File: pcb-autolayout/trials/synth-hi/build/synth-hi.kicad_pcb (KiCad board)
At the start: 4 copper layers, 52 x 40 mm, 74 parts, among them J1 CONN, U1 MCU, U11 BUF, U12 BUF, U13 BUF, U14 BUF, U15 BUF, U16 BUF, U17 BUF, U18 BUF, U19 BUF, U2 LDO, U20 BUF, U21 BUF, U22 BUF, Y1 8MHz

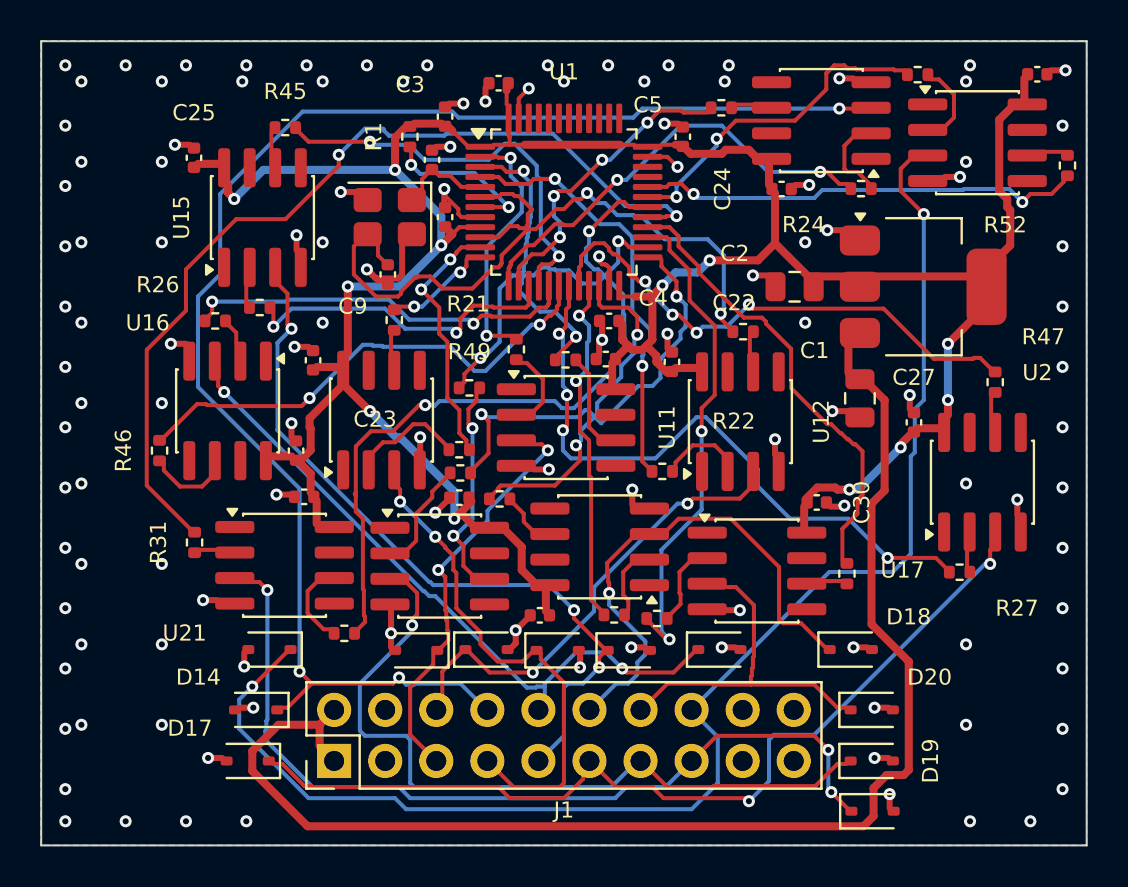
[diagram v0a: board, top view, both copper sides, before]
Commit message: synth-hi: build sau chốt chống chập — DRC 0 (hết 15 chập), 5 chân hở MCU minh bạch
Co-Authored-By: Claude Opus 5.5 <noreply@anthropic.com>
Claude-Session: https://claude.ai/code/session_012jwodCpQFB8wopi3P3TnUz
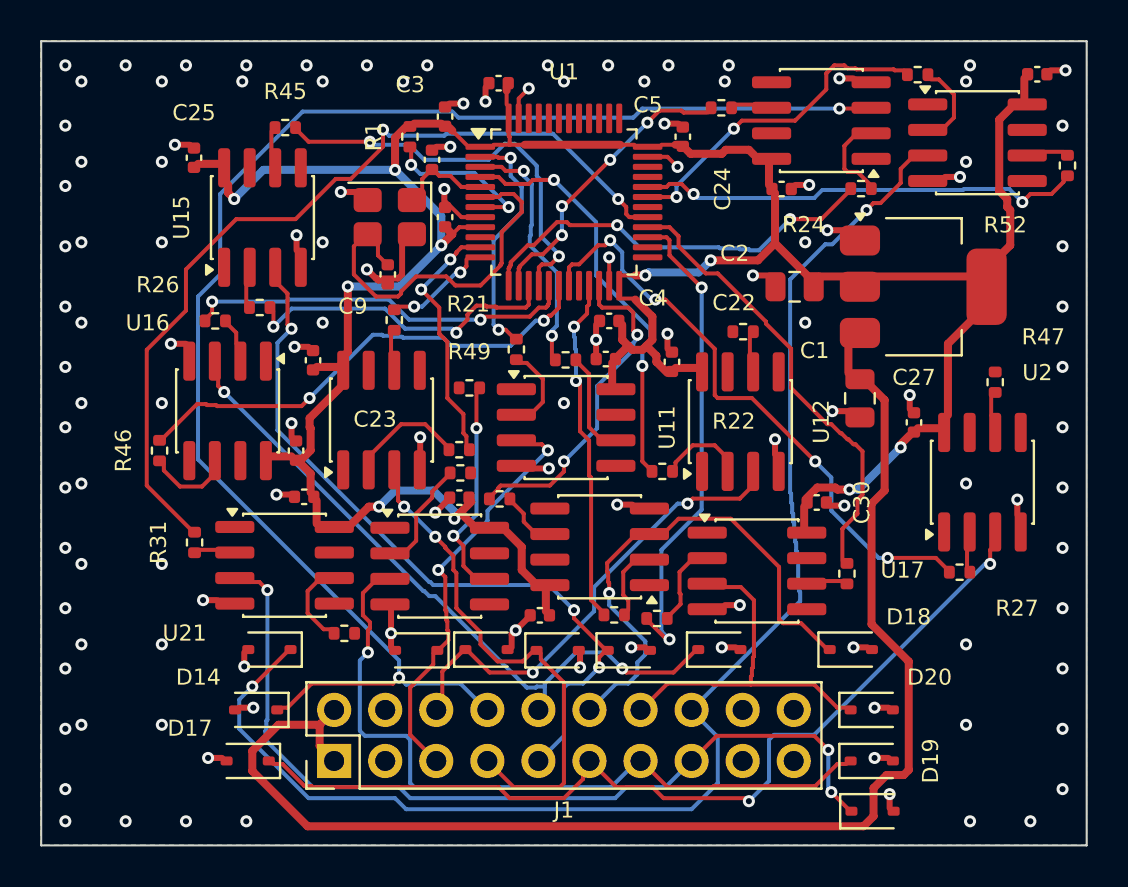
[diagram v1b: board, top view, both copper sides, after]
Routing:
- net S11_B: track 35.2 -> 0.00 mm, vias 2 -> 0
- net S7_B: track 25.7 -> 0.00 mm, vias 4 -> 0
- net S9_A: track 20.4 -> 0.00 mm, vias 2 -> 0
- net S2_B: track 17.6 -> 0.00 mm, vias 2 -> 0
- net S9_B: track 14.7 -> 0.00 mm, vias 2 -> 0
- net S11_A: track 44.9 -> 42.4 mm
- net S7_A: track 31.6 -> 29.2 mm
- net S12_OUT: track 68.8 -> 66.8 mm
- net +3V3: track 121.8 -> 120.0 mm, vias 12 -> 10
- net S4_OUT: track 71.8 -> 73.3 mm, vias 3 -> 2
- net S4_A: track 21.4 -> 19.9 mm
- net S1_B: track 13.1 -> 11.7 mm
- net S9_OUT: track 36.0 -> 35.2 mm
- net S1_A: track 11.9 -> 11.1 mm
- net S4_B: track 14.5 -> 13.8 mm
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
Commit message: T34 trên synth-hi: 5 -> 2 chân hở (vành thoát chân U1 0.8 mm), DRC 0; router in thời gian theo pha
Vành 1.6 mm tệ hơn (3 chân hở) -> engine giữ kết quả tốt nhất. Tổng 47 phút: quá chậm, đang profile.

Co-Authored-By: Claude Opus 5.5 <noreply@anthropic.com>
Claude-Session: https://claude.ai/code/session_012jwodCpQFB8wopi3P3TnUz
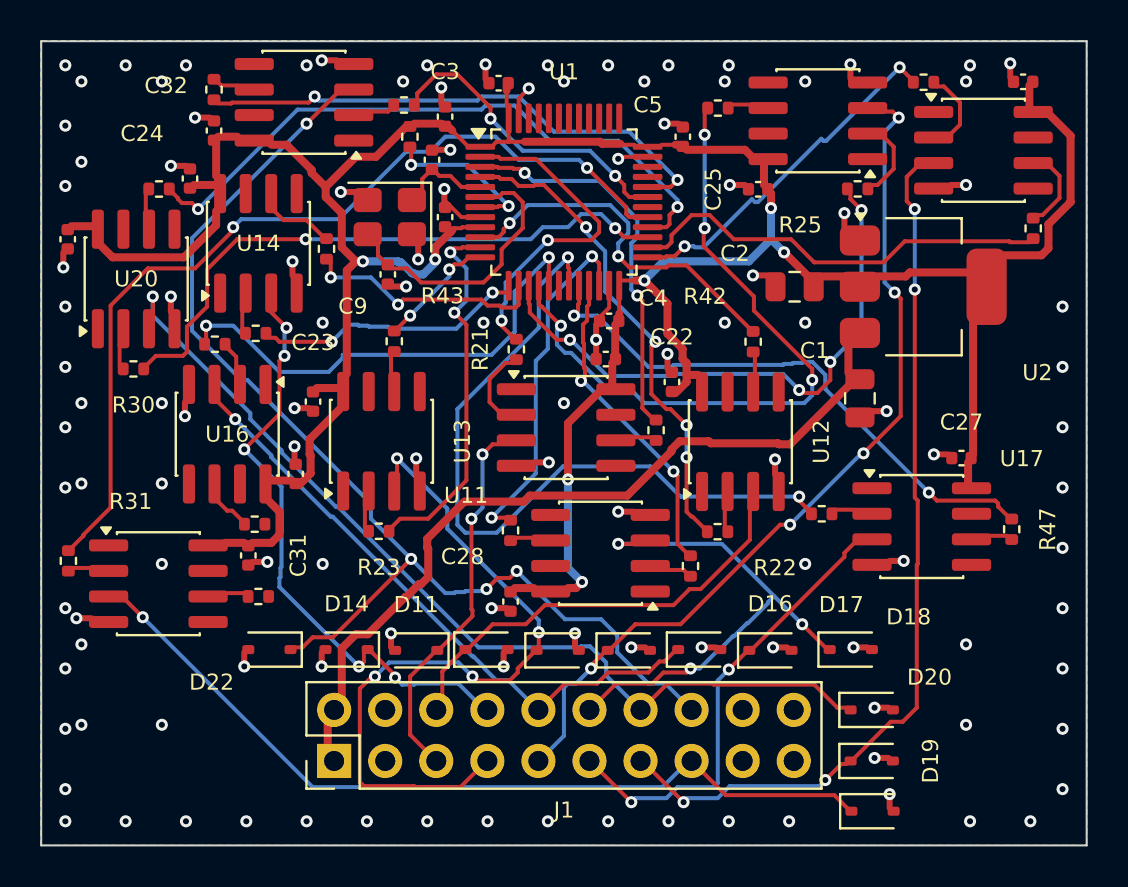
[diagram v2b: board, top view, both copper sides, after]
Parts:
- C23: renamed from C8; value 12p -> 100n
- C26: renamed from C9; value 12p -> 100n
- C7: renamed from C6; value 100n -> 1u
- C8: renamed from C7; value 1u -> 12p
- C9: renamed from C3; value 100n -> 12p
- R1: renamed from R21; value 33R -> 10k
- R22: renamed from R44; value 1k -> 33R
- R24: renamed from R43; value 1k -> 33R
- R26: renamed from R45; value 1k -> 33R
- R31: renamed from R46; value 1k -> 33R
- R32: renamed from R48; value 1k -> 33R
- R41: renamed from R30; value 33R -> 1k
- R44: renamed from R23; value 33R -> 1k
- R50: renamed from R26; value 33R -> 1k
- R51: renamed from R1; value 10k -> 1k
- R52: renamed from R25; value 33R -> 1k
- moved C6 26.5 mm to (122.8, 62.1)
- moved R29 24.4 mm to (143.9, 62.0)
- moved R51 24.1 mm to (110.8, 87.6), turned to 0 degrees
- moved U22 24.0 mm to (113.1, 63.0), turned to 180 degrees
- moved R22 21.1 mm to (133.6, 84.4), turned to 0 degrees
- moved R32 20.2 mm to (118.0, 63.2)
- moved U17 19.3 mm to (143.8, 84.1)
- moved C3 19.0 mm to (120.1, 63.8), turned to 90 degrees
- moved U21 18.9 mm to (105.8, 87.0), turned to 0 degrees
- moved C32 18.8 mm to (108.6, 64.4), turned to 90 degrees
- moved U19 16.5 mm to (146.9, 65.4), turned to 0 degrees
- moved R27 16.3 mm to (138.8, 83.5)
- moved C25 15.8 mm to (135.7, 67.4), turned to 180 degrees
- moved C24 14.5 mm to (107.4, 66.8)
- moved R21 14.1 mm to (123.6, 75.3), turned to -90 degrees
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- renumbered C4 to C21, C5 to C22, C26 to C24, C30 to C25, C21 to C28, C32 to C29, C29 to C3, C25 to C30, C23 to C31, C31 to C32, C22 to C4, C24 to C5, C28 to C6, D22 to D11, D11 to D12, D12 to D13, D13 to D15, D15 to D16, D16 to D17, D17 to D22, R28 to R21, R29 to R23, R32 to R25, R24 to R27, R22 to R28, R27 to R29, R31 to R30, R50 to R42, R49 to R43, R42 to R45, R51 to R46, R41 to R48, R52 to R49, U18 to U11, U20 to U12, U11 to U13, U13 to U14, U14 to U15, U21 to U16, U22 to U17, U12 to U18, U17 to U19, U16 to U20, U15 to U21, U19 to U22
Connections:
- C23 pad 1: OSC_IN -> +3V3
- C26 pad 1: OSC_OUT -> +3V3
- C8 pad 1: +3V3 -> OSC_IN
- C9 pad 1: +3V3 -> OSC_OUT
- D11 pad 1: S12_OUT -> S1_OUT
- D12 pad 1: S1_OUT -> S2_OUT
- D13 pad 1: S2_OUT -> S3_OUT
- D15 pad 1: S3_OUT -> S5_OUT
- D16 pad 1: S5_OUT -> S6_OUT
- D17 pad 1: S6_OUT -> S7_OUT
- D22 pad 1: S7_OUT -> S12_OUT
- R1 pad 1: S1_A -> NRST
- R1 pad 2: S1_IN -> +3V3
- R21 pad 1: S8_A -> S1_A
- R21 pad 2: S8_IN -> S1_IN
- R22 pad 1: S4_FB -> S2_A
- R22 pad 2: S4_B -> S2_IN
- R23 pad 1: S9_A -> S3_A
- R23 pad 2: S9_IN -> S3_IN
- R24 pad 1: S3_FB -> S4_A
- R24 pad 2: S3_B -> S4_IN
- R25 pad 1: S12_A -> S5_A
- R25 pad 2: S12_IN -> S5_IN
- R26 pad 1: S5_FB -> S6_A
- R26 pad 2: S5_B -> S6_IN
- R27 pad 1: S4_A -> S7_A
- R27 pad 2: S4_IN -> S7_IN
- R28 pad 1: S2_A -> S8_A
- R28 pad 2: S2_IN -> S8_IN
- R29 pad 1: S7_A -> S9_A
- R29 pad 2: S7_IN -> S9_IN
- R30 pad 1: S11_A -> S10_A
- R30 pad 2: S11_IN -> S10_IN
- R31 pad 1: S6_FB -> S11_A
- R31 pad 2: S6_B -> S11_IN
- R32 pad 1: S8_FB -> S12_A
- R32 pad 2: S8_B -> S12_IN
- R41 pad 1: S10_A -> S1_FB
- R41 pad 2: S10_IN -> S1_B
- R42 pad 1: S10_FB -> S2_FB
- R42 pad 2: S10_B -> S2_B
- R43 pad 1: S9_FB -> S3_FB
- R43 pad 2: S9_B -> S3_B
- R44 pad 1: S3_A -> S4_FB
- R44 pad 2: S3_IN -> S4_B
- R45 pad 1: S2_FB -> S5_FB
- R45 pad 2: S2_B -> S5_B
- R46 pad 1: S11_FB -> S6_FB
- R46 pad 2: S11_B -> S6_B
- R48 pad 1: S1_FB -> S8_FB
- R48 pad 2: S1_B -> S8_B
- R49 pad 1: S12_FB -> S9_FB
- R49 pad 2: S12_B -> S9_B
- R50 pad 1: S6_A -> S10_FB
- R50 pad 2: S6_IN -> S10_B
- R51 pad 1: NRST -> S11_FB
- R51 pad 2: +3V3 -> S11_B
- R52 pad 1: S5_A -> S12_FB
- R52 pad 2: S5_IN -> S12_B
- U11 pad 2: S8_IN -> S1_IN
- U11 pad 3: S8_OUT -> S1_OUT
- U11 pad 6: S8_FB -> S1_FB
- U12 pad 2: S10_IN -> S2_IN
- U12 pad 3: S10_OUT -> S2_OUT
- U12 pad 6: S10_FB -> S2_FB
- U13 pad 2: S1_IN -> S3_IN
- U13 pad 3: S1_OUT -> S3_OUT
- U13 pad 6: S1_FB -> S3_FB
- U14 pad 2: S3_IN -> S4_IN
- U14 pad 3: S3_OUT -> S4_OUT
- U14 pad 6: S3_FB -> S4_FB
- U15 pad 2: S4_IN -> S5_IN
- U15 pad 3: S4_OUT -> S5_OUT
- U15 pad 6: S4_FB -> S5_FB
- U16 pad 2: S11_IN -> S6_IN
- U16 pad 3: S11_OUT -> S6_OUT
- U16 pad 6: S11_FB -> S6_FB
- U17 pad 2: S12_IN -> S7_IN
- U17 pad 3: S12_OUT -> S7_OUT
- U17 pad 6: S12_FB -> S7_FB
- U18 pad 2: S2_IN -> S8_IN
- U18 pad 3: S2_OUT -> S8_OUT
- U18 pad 6: S2_FB -> S8_FB
- U19 pad 2: S7_IN -> S9_IN
- U19 pad 3: S7_OUT -> S9_OUT
- U19 pad 6: S7_FB -> S9_FB
- U20 pad 2: S6_IN -> S10_IN
- U20 pad 3: S6_OUT -> S10_OUT
- U20 pad 6: S6_FB -> S10_FB
- U21 pad 2: S5_IN -> S11_IN
- U21 pad 3: S5_OUT -> S11_OUT
- U21 pad 6: S5_FB -> S11_FB
- U22 pad 2: S9_IN -> S12_IN
- U22 pad 3: S9_OUT -> S12_OUT
- U22 pad 6: S9_FB -> S12_FB
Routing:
- net S4_OUT: track 73.3 -> 28.8 mm, vias 2 -> 5
- net S10_OUT: track 16.8 -> 45.1 mm, vias 0 -> 1
- net S7_B: track 0.00 -> 27.3 mm, vias 0 -> 2
- net VIN: track 64.3 -> 37.7 mm
- net S6_B: track 23.3 -> 0.00 mm, vias 2 -> 0
- net S7_OUT: track 44.3 -> 21.4 mm
- net S9_B: track 0.00 -> 20.6 mm
- net S2_B: track 0.00 -> 17.7 mm, vias 0 -> 2
- net S9_A: track 0.00 -> 16.8 mm, vias 0 -> 2
- net S5_B: track 19.7 -> 33.2 mm, vias 2 -> 4
- net S5_A: track 15.4 -> 27.8 mm, vias 2 -> 4
- net S3_OUT: track 23.6 -> 34.4 mm, vias 2 -> 4
- net S12_OUT: track 66.8 -> 56.5 mm, vias 2 -> 4
- net S10_B: track 21.9 -> 31.4 mm, vias 0 -> 2
- net S9_OUT: track 35.2 -> 42.9 mm, vias 1 -> 4
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
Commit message: bench R sau sửa review: bcm4l 16/16; synth-hi hết chập (DRC 21 -> 0) đổi 2 chân hở; synth-lo TỤT 0 -> 1 hở (đang truy)
bench ghi build/run.log từng trial để truy hồi quy.

Co-Authored-By: Claude Opus 5.5 <noreply@anthropic.com>
Claude-Session: https://claude.ai/code/session_012jwodCpQFB8wopi3P3TnUz
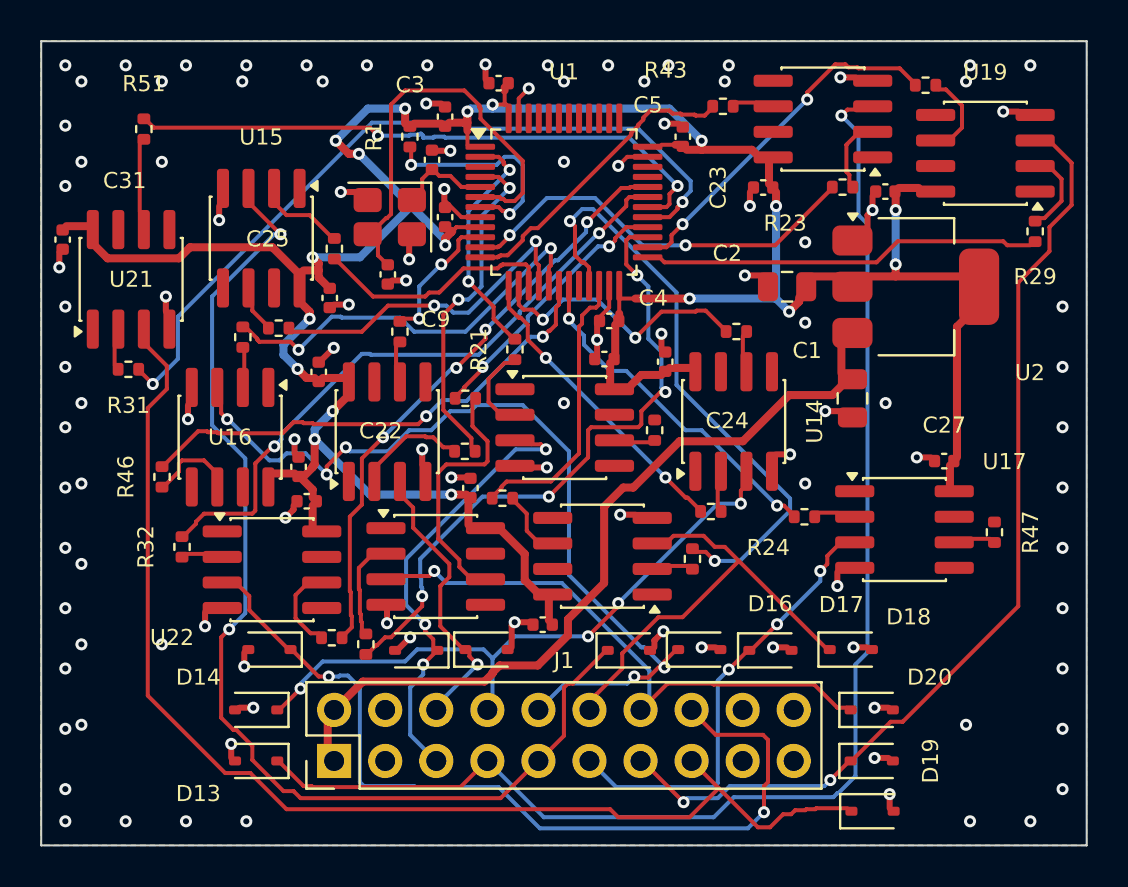
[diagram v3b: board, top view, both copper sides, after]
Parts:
- C3: renamed from C8; value 12p -> 100n
- C30: renamed from C7; value 1u -> 100n
- C7: renamed from C3; value 100n -> 1u
- C9: renamed from C23; value 100n -> 12p
- R1: renamed from R43; value 1k -> 10k
- R25: renamed from R51; value 1k -> 33R
- R29: renamed from R49; value 1k -> 33R
- R30: renamed from R44; value 1k -> 33R
- R32: renamed from R52; value 1k -> 33R
- R42: renamed from R23; value 33R -> 1k
- R49: renamed from R29; value 33R -> 1k
- R50: renamed from R1; value 10k -> 1k
- R51: renamed from R30; value 33R -> 1k
- R52: renamed from R24; value 33R -> 1k
- moved R32 22.8 mm to (107.0, 85.2)
- moved R30 19.8 mm to (116.1, 90.0), turned to 90 degrees
- moved C27 19.3 mm to (144.9, 80.9)
- moved C32 19.0 mm to (113.2, 82.9), turned to 180 degrees
- moved R25 17.7 mm to (114.6, 70.3), turned to 90 degrees
- moved R22 17.5 mm to (121.1, 80.4)
- moved U12 16.9 mm to (117.2, 79.4), turned to 90 degrees
- moved U22 16.2 mm to (111.5, 86.3), turned to 0 degrees
- moved R52 15.6 mm to (114.5, 89.7), turned to 0 degrees
- moved C26 15.3 mm to (112.8, 81.2)
- moved R46 14.3 mm to (106.0, 81.7), turned to 90 degrees
- moved C29 13.8 mm to (142.0, 67.5)
- moved C30 13.5 mm to (121.3, 82.2)
- moved R50 13.3 mm to (121.1, 77.8), turned to 180 degrees
- moved R51 11.9 mm to (105.1, 64.4), turned to 90 degrees
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- renumbered C31 to C22, C25 to C23, C22 to C24, C26 to C25, C24 to C26, C29 to C27, C27 to C29, C30 to C31, C9 to C8, D12 to D11, D13 to D12, D14 to D13, D22 to D14, D11 to D22, R32 to R22, R25 to R23, R22 to R24, R45 to R43, R42 to R44, R46 to R45, R50 to R46, U22 to U12, U15 to U13, U12 to U14, U16 to U15, U21 to U16, U13 to U20, U20 to U21, U14 to U22
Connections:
- C3 pad 1: OSC_IN -> +3V3
- C8 pad 1: OSC_OUT -> OSC_IN
- C9 pad 1: +3V3 -> OSC_OUT
- D11 pad 1: S2_OUT -> S1_OUT
- D12 pad 1: S3_OUT -> S2_OUT
- D13 pad 1: S4_OUT -> S3_OUT
- D14 pad 1: S12_OUT -> S4_OUT
- D22 pad 1: S1_OUT -> S12_OUT
- R1 pad 1: S3_FB -> NRST
- R1 pad 2: S3_B -> +3V3
- R22 pad 1: S12_A -> S2_A
- R22 pad 2: S12_IN -> S2_IN
- R23 pad 1: S5_A -> S3_A
- R23 pad 2: S5_IN -> S3_IN
- R24 pad 1: S2_A -> S4_A
- R24 pad 2: S2_IN -> S4_IN
- R25 pad 1: S11_FB -> S5_A
- R25 pad 2: S11_B -> S5_IN
- R29 pad 1: S9_FB -> S9_A
- R29 pad 2: S9_B -> S9_IN
- R30 pad 1: S4_FB -> S10_A
- R30 pad 2: S4_B -> S10_IN
- R32 pad 1: S12_FB -> S12_A
- R32 pad 2: S12_B -> S12_IN
- R42 pad 1: S3_A -> S2_FB
- R42 pad 2: S3_IN -> S2_B
- R43 pad 1: S5_FB -> S3_FB
- R43 pad 2: S5_B -> S3_B
- R44 pad 1: S2_FB -> S4_FB
- R44 pad 2: S2_B -> S4_B
- R45 pad 1: S6_FB -> S5_FB
- R45 pad 2: S6_B -> S5_B
- R46 pad 1: S10_FB -> S6_FB
- R46 pad 2: S10_B -> S6_B
- R49 pad 1: S9_A -> S9_FB
- R49 pad 2: S9_IN -> S9_B
- R50 pad 1: NRST -> S10_FB
- R50 pad 2: +3V3 -> S10_B
- R51 pad 1: S10_A -> S11_FB
- R51 pad 2: S10_IN -> S11_B
- R52 pad 1: S4_A -> S12_FB
- R52 pad 2: S4_IN -> S12_B
- U12 pad 2: S12_IN -> S2_IN
- U12 pad 3: S12_OUT -> S2_OUT
- U12 pad 6: S12_FB -> S2_FB
- U13 pad 2: S5_IN -> S3_IN
- U13 pad 3: S5_OUT -> S3_OUT
- U13 pad 6: S5_FB -> S3_FB
- U14 pad 2: S2_IN -> S4_IN
- U14 pad 3: S2_OUT -> S4_OUT
- U14 pad 6: S2_FB -> S4_FB
- U15 pad 2: S6_IN -> S5_IN
- U15 pad 3: S6_OUT -> S5_OUT
- U15 pad 6: S6_FB -> S5_FB
- U16 pad 2: S11_IN -> S6_IN
- U16 pad 3: S11_OUT -> S6_OUT
- U16 pad 6: S11_FB -> S6_FB
- U20 pad 2: S3_IN -> S10_IN
- U20 pad 3: S3_OUT -> S10_OUT
- U20 pad 6: S3_FB -> S10_FB
- U21 pad 2: S10_IN -> S11_IN
- U21 pad 3: S10_OUT -> S11_OUT
- U21 pad 6: S10_FB -> S11_FB
- U22 pad 2: S4_IN -> S12_IN
- U22 pad 3: S4_OUT -> S12_OUT
- U22 pad 6: S4_FB -> S12_FB
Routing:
- net S3_OUT: track 34.4 -> 65.1 mm, vias 4 -> 1
- net S11_B: track 0.00 -> 29.4 mm, vias 0 -> 2
- net S7_B: track 27.3 -> 0.00 mm, vias 2 -> 0
- net S6_B: track 0.00 -> 23.8 mm, vias 0 -> 2
- net S7_A: track 36.3 -> 16.3 mm
- net S10_B: track 31.4 -> 12.5 mm
- net S1_B: track 18.6 -> 0.00 mm, vias 2 -> 0
- net S11_OUT: track 40.4 -> 58.7 mm, vias 1 -> 0
- net S10_OUT: track 45.1 -> 26.9 mm
- net S5_B: track 33.2 -> 16.0 mm, vias 4 -> 2
- net S5_A: track 27.8 -> 11.1 mm, vias 4 -> 0
- net S12_A: track 14.6 -> 31.1 mm
- net S12_OUT: track 56.5 -> 41.8 mm, vias 4 -> 2
- net S8_A: track 15.1 -> 29.3 mm
- net S6_OUT: track 29.4 -> 42.6 mm, vias 1 -> 5
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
